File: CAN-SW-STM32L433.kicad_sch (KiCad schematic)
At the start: 8 parts, among them U1 STM32L433CCTx

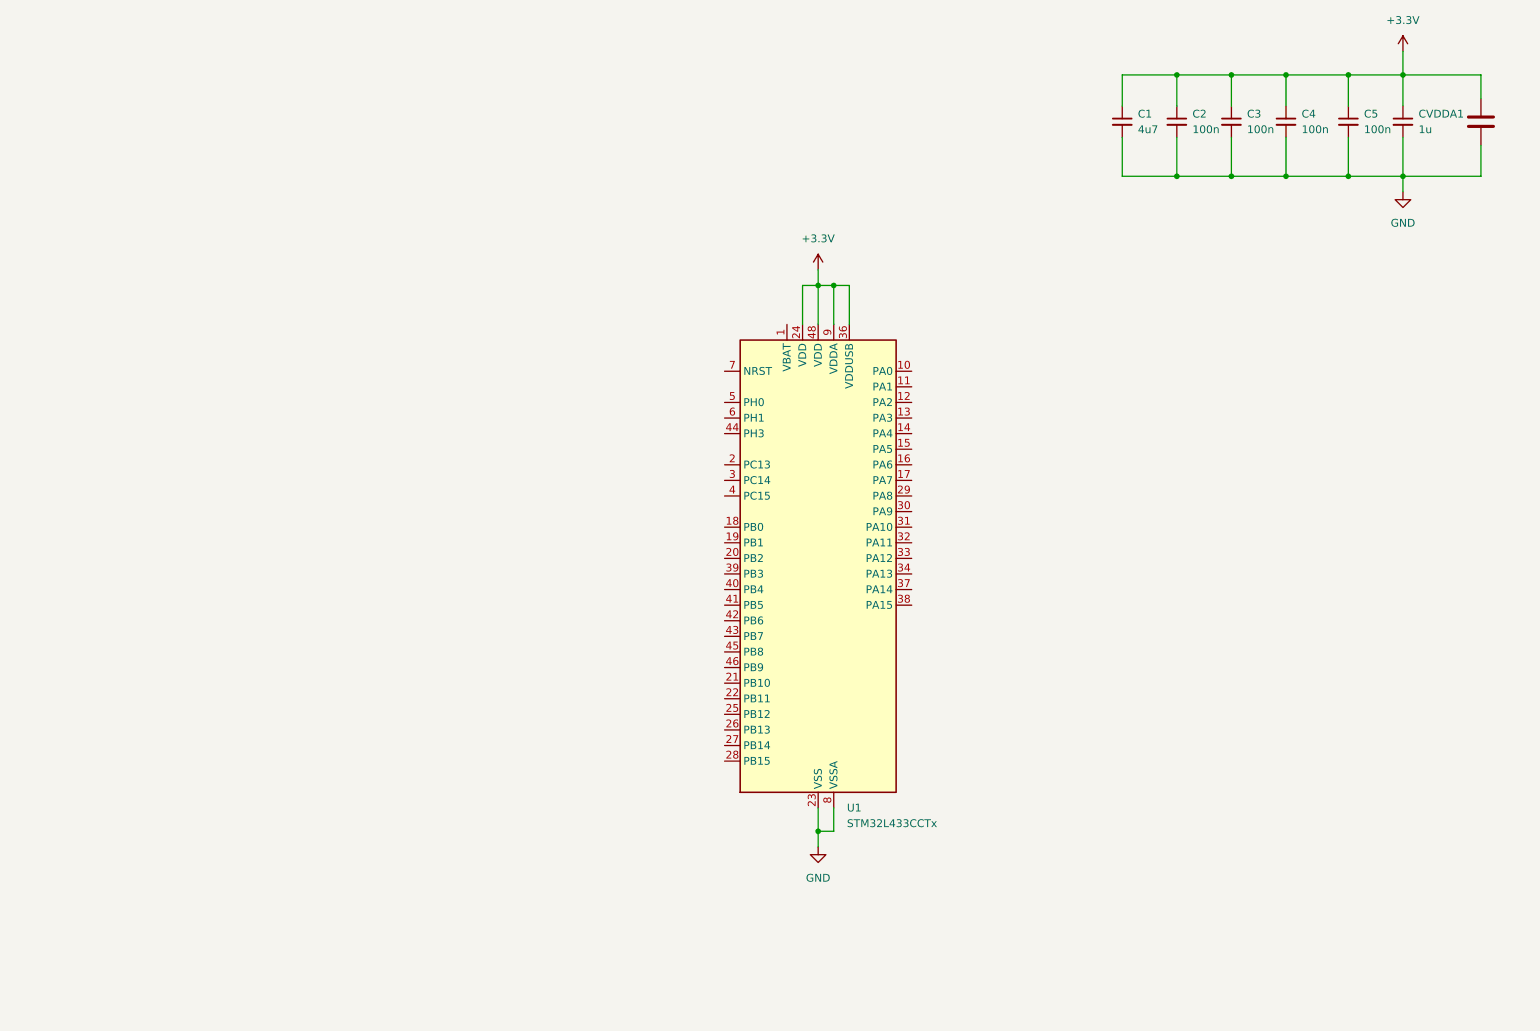
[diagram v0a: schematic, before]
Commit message: still adding parts, working on basic layout
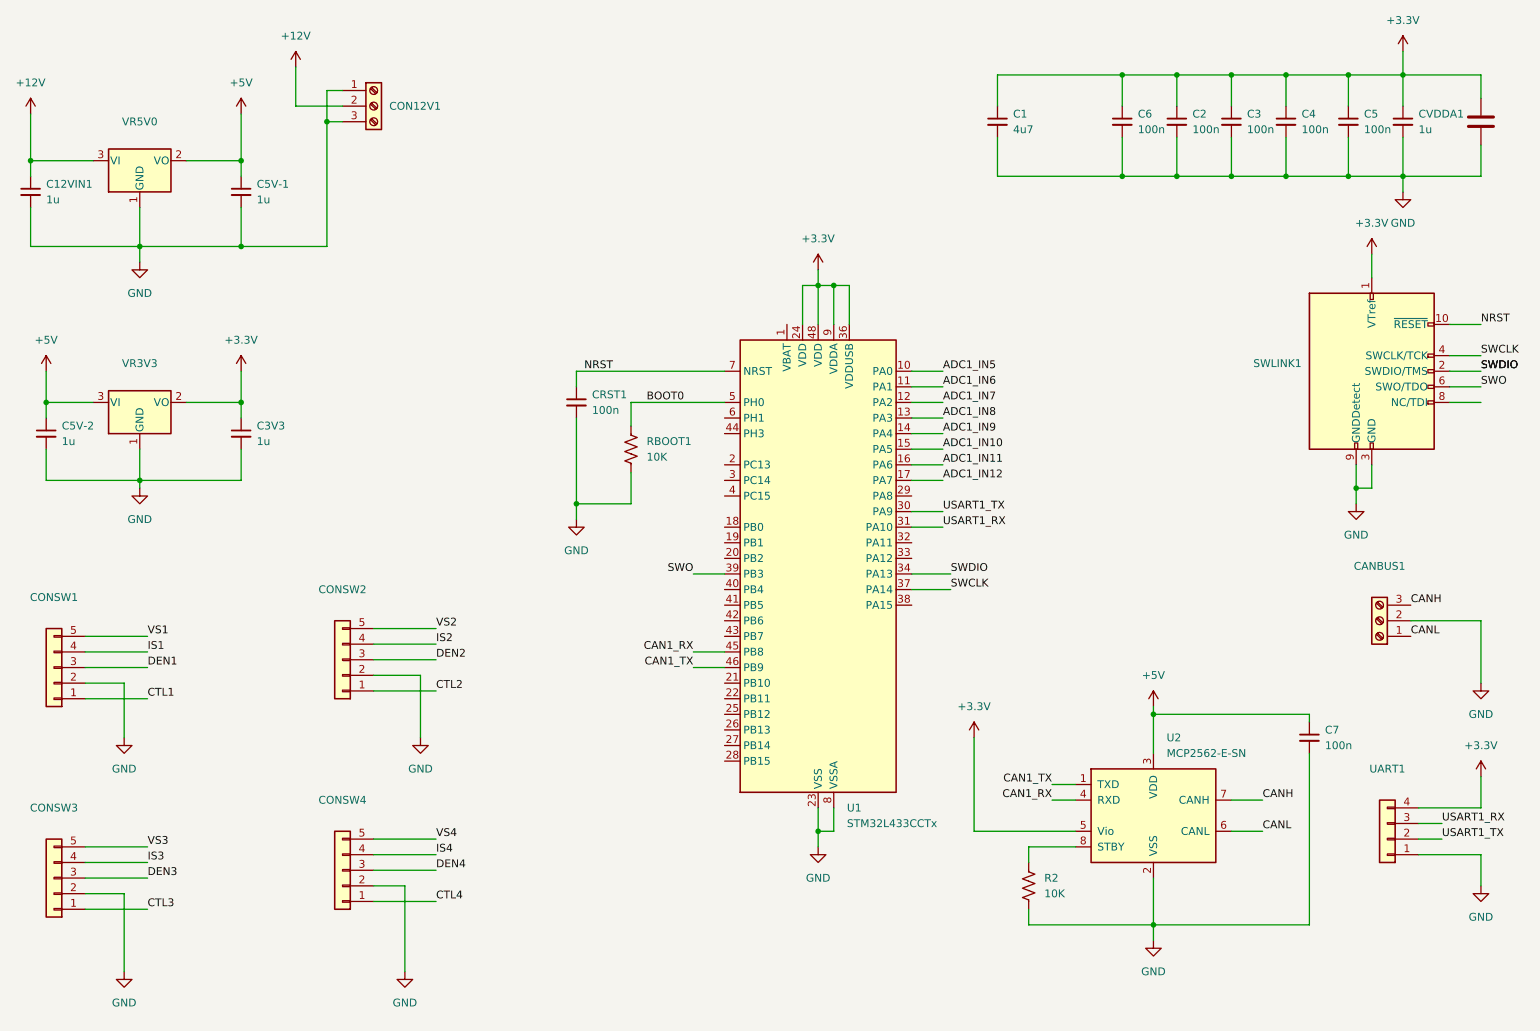
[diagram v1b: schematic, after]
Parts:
- added C12VIN1: 1u, Capacitor_SMD:C_1206_3216Metric_Pad1.33x1.80mm_HandSolder, symbol Device:C_Small
- added C3V3, C5V-1, C5V-2: 1u, Capacitor_SMD:C_0805_2012Metric_Pad1.18x1.45mm_HandSolder, symbol Device:C_Small
- added C6, C7, CRST1: 100n, Capacitor_SMD:C_0603_1608Metric_Pad1.08x0.95mm_HandSolder, symbol Device:C_Small
- added CANBUS1: Screw_Terminal_01x03, TerminalBlock_Phoenix:TerminalBlock_Phoenix_MKDS-1,5-3-5.08_1x03_P5.08mm_Horizontal, symbol Connector:Screw_Terminal_01x03
- added CON12V1: CENTER+, TerminalBlock_Phoenix:TerminalBlock_Phoenix_MKDS-1,5-3-5.08_1x03_P5.08mm_Horizontal, symbol Connector:Screw_Terminal_01x03
- added CONSW1, CONSW2, CONSW3, CONSW4: Conn_01x05, Connector_PinSocket_2.54mm:PinSocket_1x05_P2.54mm_Horizontal, symbol Connector_Generic:Conn_01x05
- added R2, RBOOT1: 10K, Resistor_SMD:R_0603_1608Metric_Pad0.98x0.95mm_HandSolder, symbol Device:R_US
- added SWLINK1: Conn_ARM_JTAG_SWD_10, Connector_PinHeader_1.27mm:PinHeader_2x05_P1.27mm_Horizontal, symbol Connector:Conn_ARM_JTAG_SWD_10
- added U2: MCP2562-E-SN, Package_SO:SOIC-8_3.9x4.9mm_P1.27mm, symbol Interface_CAN_LIN:MCP2562-E-SN
- added UART1: Conn_01x04, Connector_PinHeader_1.27mm:PinHeader_1x04_P1.27mm_Horizontal, symbol Connector_Generic:Conn_01x04
- added VR3V3: TLV1117-33, Package_TO_SOT_SMD:SOT-223-3_TabPin2, symbol Regulator_Linear:TLV1117-33
- added VR5V0: TLV1117-50, Package_TO_SOT_SMD:SOT-223-3_TabPin2, symbol Regulator_Linear:TLV1117-50
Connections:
- net +3.3V: now also C3V3.1, C6.1, SWLINK1.1 (VTref), U2.5 (Vio), UART1.4 (Pin_4), VR3V3.2 (VO)
- net GND: now also C12VIN1.2, C3V3.2, C5V-1.2, C5V-2.2, C6.2, C7.2, CANBUS1.2 (Pin_2), CON12V1.1 (Pin_1), CON12V1.3 (Pin_3), CONSW1.2 (Pin_2), CONSW2.2 (Pin_2), CONSW3.2 (Pin_2), CONSW4.2 (Pin_2), CRST1.2, R2.2, RBOOT1.2, SWLINK1.3 (GND), SWLINK1.5 (GND), SWLINK1.9 (GNDDetect), U2.2 (VSS), UART1.1 (Pin_1), VR3V3.1 (GND), VR5V0.1 (GND)
- net ADC1_IN5: now reaches U1.10 (PA0)
- net ADC1_IN6: now reaches U1.11 (PA1)
- net ADC1_IN7: now reaches U1.12 (PA2)
- net ADC1_IN8: now reaches U1.13 (PA3)
- net ADC1_IN9: now reaches U1.14 (PA4)
- net ADC1_IN10: now reaches U1.15 (PA5)
- net ADC1_IN11: now reaches U1.16 (PA6)
- net ADC1_IN12: now reaches U1.17 (PA7)
- net USART1_TX: now reaches U1.30 (PA9)
- net USART1_TX: now also UART1.2 (Pin_2)
- net USART1_RX: now reaches U1.31 (PA10)
- net USART1_RX: now also UART1.3 (Pin_3)
- net SWDIO: now reaches U1.34 (PA13)
- net SWDIO: now also SWLINK1.2 (SWDIO/TMS)
- net SWCLK: now reaches U1.37 (PA14)
- net SWCLK: now also SWLINK1.4 (SWCLK/TCK)
- net SWO: now reaches U1.39 (PB3)
- net SWO: now also SWLINK1.6 (SWO/TDO)
- net CAN1_RX: now reaches U1.45 (PB8)
- net CAN1_RX: now also U2.4 (RXD)
- net CAN1_TX: now reaches U1.46 (PB9)
- net CAN1_TX: now also U2.1 (TXD)
- net BOOT0: now reaches U1.5 (PH0)
- net BOOT0: now also RBOOT1.1
- net NRST: now reaches U1.7 (NRST)
- net NRST: now also CRST1.1, SWLINK1.10 (~{RESET})
- new net: R2.1, U2.8 (STBY)
- new net +12V: C12VIN1.1, CON12V1.2 (Pin_2), VR5V0.3 (VI)
- new net +5V: C5V-1.1, C5V-2.1, C7.1, U2.3 (VDD), VR3V3.3 (VI), VR5V0.2 (VO)
- new net CANH: CANBUS1.3 (Pin_3), U2.7 (CANH)
- new net CANL: CANBUS1.1 (Pin_1), U2.6 (CANL)
- new net CTL1: CONSW1.1 (Pin_1)
- new net CTL2: CONSW2.1 (Pin_1)
- new net CTL3: CONSW3.1 (Pin_1)
- new net CTL4: CONSW4.1 (Pin_1)
- new net DEN1: CONSW1.3 (Pin_3)
- new net DEN2: CONSW2.3 (Pin_3)
- new net DEN3: CONSW3.3 (Pin_3)
- new net DEN4: CONSW4.3 (Pin_3)
- new net IS1: CONSW1.4 (Pin_4)
- new net IS2: CONSW2.4 (Pin_4)
- new net IS3: CONSW3.4 (Pin_4)
- new net IS4: CONSW4.4 (Pin_4)
- new net VS1: CONSW1.5 (Pin_5)
- new net VS2: CONSW2.5 (Pin_5)
- new net VS3: CONSW3.5 (Pin_5)
- new net VS4: CONSW4.5 (Pin_5)
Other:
- company: (none) -> Gordon McLellan
- title: (none) -> CAN-STM32L433
- moved on the sheet: C1

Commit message: almost done adding parts, working more on layout
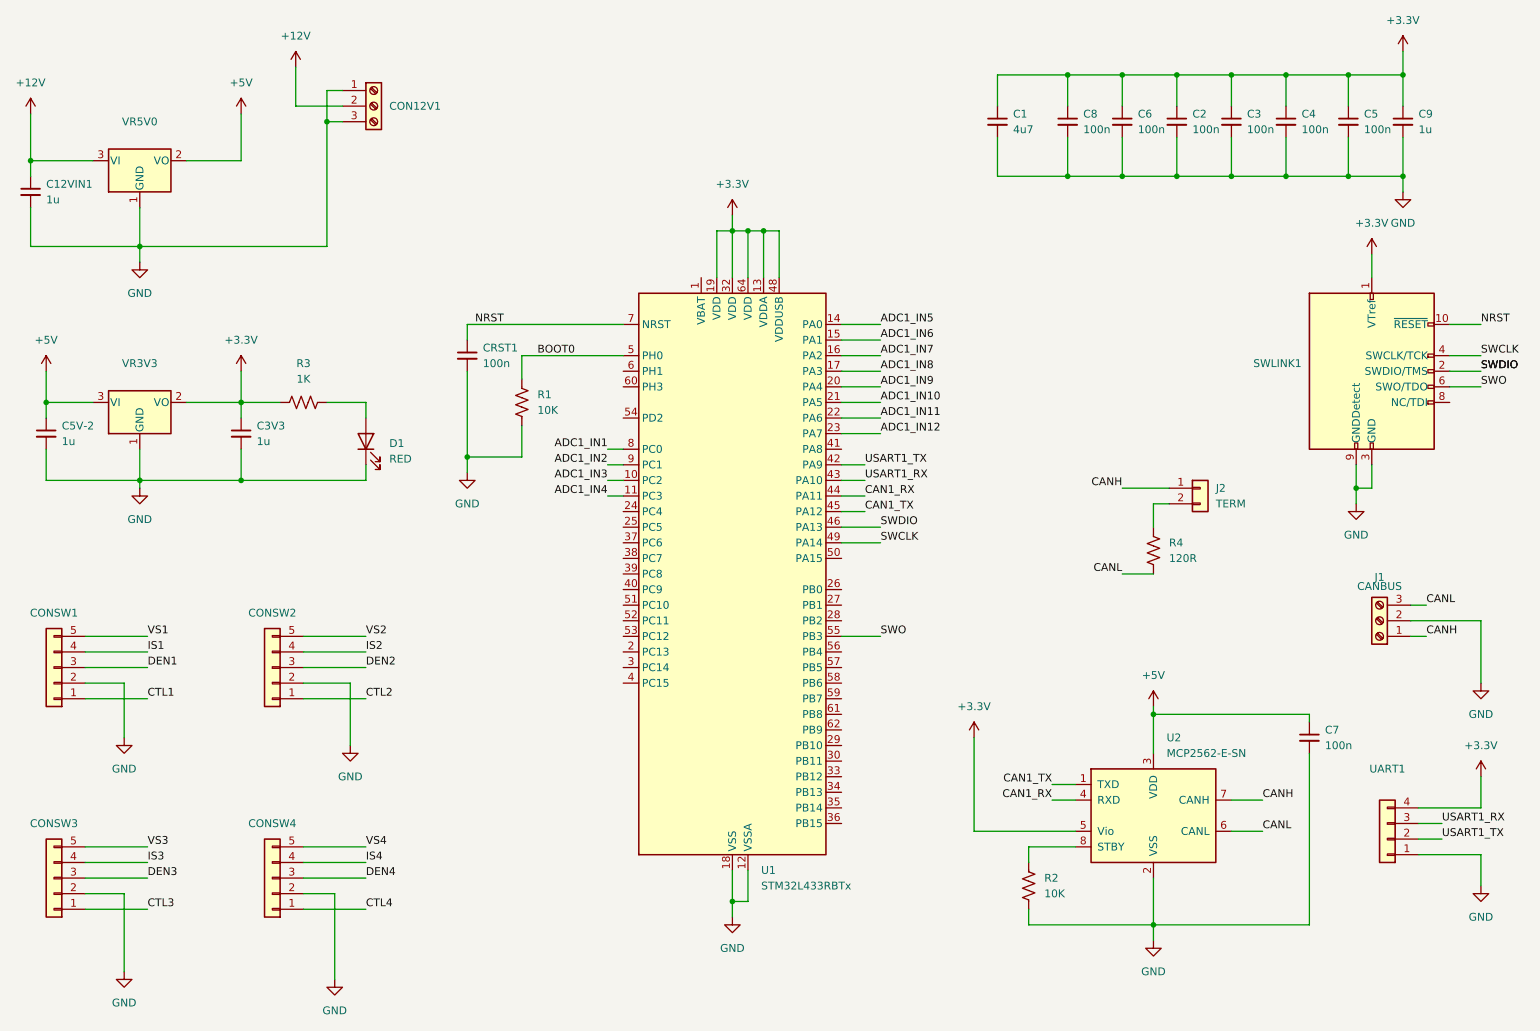
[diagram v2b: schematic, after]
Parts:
- removed C5V-1: 1u, Capacitor_SMD:C_0805_2012Metric_Pad1.18x1.45mm_HandSolder, symbol Device:C_Small
- removed CVREF1: 100n, Capacitor_SMD:C_0603_1608Metric_Pad1.08x0.95mm_HandSolder, symbol Device:C
- removed U1: STM32L433CCTx, Package_QFP:LQFP-48_7x7mm_P0.5mm, symbol MCU_ST_STM32L4:STM32L433CCTx
- added C8: 100n, Capacitor_SMD:C_0603_1608Metric_Pad1.08x0.95mm_HandSolder, symbol Device:C_Small
- added D1: RED, LED_THT:LED_D5.0mm_Clear, symbol Device:LED
- added J2: TERM, Connector_PinHeader_1.27mm:PinHeader_1x02_P1.27mm_Vertical, symbol Connector_Generic:Conn_01x02
- added R3: 1K, Resistor_SMD:R_0603_1608Metric_Pad0.98x0.95mm_HandSolder, symbol Device:R_US
- added R4: 120R, Resistor_THT:R_Axial_DIN0207_L6.3mm_D2.5mm_P7.62mm_Horizontal, symbol Device:R_US
- added U1: STM32L433RBTx, Package_QFP:LQFP-64_10x10mm_P0.5mm, symbol MCU_ST_STM32L4:STM32L433RBTx
- CON12V1: footprint TerminalBlock_Phoenix:TerminalBlock_Phoenix_MKDS-1,5-3-5.08_1x03_P5.08mm_Horizontal -> TerminalBlock_Phoenix:TerminalBlock_Phoenix_MKDS-1,5-3_1x03_P5.00mm_Horizontal
- CONSW1, CONSW2, CONSW3, CONSW4: footprint Connector_PinSocket_2.54mm:PinSocket_1x05_P2.54mm_Horizontal -> Connector_PinHeader_2.54mm:PinHeader_1x05_P2.54mm_Horizontal
- J1: renamed from CANBUS1; value Screw_Terminal_01x03 -> CANBUS; footprint TerminalBlock_Phoenix:TerminalBlock_Phoenix_MKDS-1,5-3-5.08_1x03_P5.08mm_Horizontal -> TerminalBlock_Phoenix:TerminalBlock_Phoenix_MKDS-1,5-3_1x03_P5.00mm_Horizontal
- renumbered CVDDA1 to C9, RBOOT1 to R1
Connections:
- net +3.3V: now also C8.1, R3.1, U1.13 (VDDA), U1.19 (VDD), U1.32 (VDD), U1.48 (VDDUSB), U1.64 (VDD)
- net ADC1_IN10: now also U1.21 (PA5)
- net ADC1_IN11: now also U1.22 (PA6)
- net ADC1_IN12: now also U1.23 (PA7)
- net ADC1_IN5: now also U1.14 (PA0)
- net ADC1_IN6: now also U1.15 (PA1)
- net ADC1_IN7: now also U1.16 (PA2)
- net ADC1_IN8: now also U1.17 (PA3)
- net ADC1_IN9: now also U1.20 (PA4)
- net BOOT0: now also U1.5 (PH0)
- net CAN1_RX: now also U1.44 (PA11)
- net CAN1_TX: now also U1.45 (PA12)
- net CANH: now also J1.1 (Pin_1), J2.1 (Pin_1); no longer J1.3 (Pin_3)
- net CANL: now also J1.3 (Pin_3), R4.2; no longer J1.1 (Pin_1)
- net GND: now also C8.2, D1.1 (K), U1.12 (VSSA), U1.18 (VSS), U1.31 (VSS), U1.47 (VSS), U1.63 (VSS)
- net NRST: now also U1.7 (NRST)
- net SWCLK: now also U1.49 (PA14)
- net SWDIO: now also U1.46 (PA13)
- net SWO: now also U1.55 (PB3)
- net USART1_RX: now also U1.43 (PA10)
- net USART1_TX: now also U1.42 (PA9)
- new net: J2.2 (Pin_2), R4.1
- new net: D1.2 (A), R3.2
- new net ADC1_IN1: U1.8 (PC0)
- new net ADC1_IN2: U1.9 (PC1)
- new net ADC1_IN3: U1.10 (PC2)
- new net ADC1_IN4: U1.11 (PC3)
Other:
- moved on the sheet: CONSW2, CONSW4, CRST1, R1

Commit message: more progress on the layout, fixed connector sizes for uart and swlink
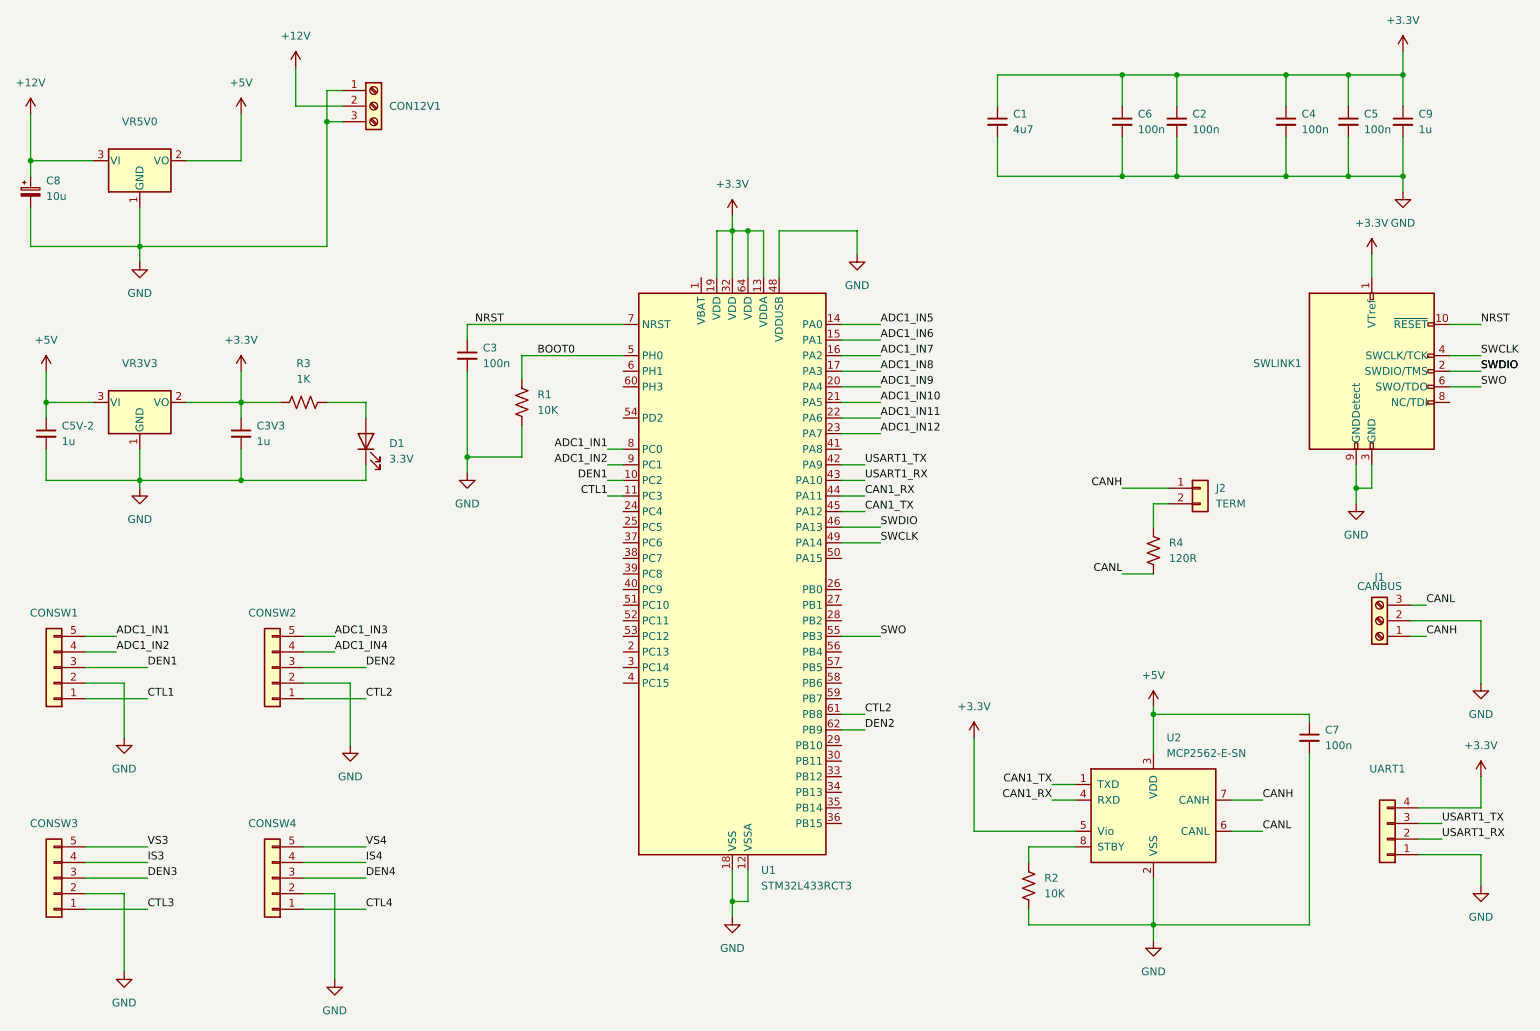
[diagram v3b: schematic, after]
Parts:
- removed C12VIN1: 1u, Capacitor_SMD:C_1206_3216Metric_Pad1.33x1.80mm_HandSolder, symbol Device:C_Small
- removed C3, C8: 100n, Capacitor_SMD:C_0603_1608Metric_Pad1.08x0.95mm_HandSolder, symbol Device:C_Small
- added C8: 10u, Capacitor_THT:CP_Radial_D5.0mm_P2.50mm, symbol Device:C_Polarized_Small
- D1: value RED -> 3.3V
- SWLINK1: footprint Connector_PinHeader_1.27mm:PinHeader_2x05_P1.27mm_Horizontal -> Connector_PinHeader_2.54mm:PinHeader_2x05_P2.54mm_Horizontal
- U1: value STM32L433RBTx -> STM32L433RCT3
- UART1: footprint Connector_PinHeader_1.27mm:PinHeader_1x04_P1.27mm_Horizontal -> Connector_PinHeader_2.54mm:PinHeader_1x04_P2.54mm_Horizontal
- renumbered CRST1 to C3
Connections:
- net IS1 is gone; now on net ADC1_IN2: CONSW1.4 (Pin_4)
- net IS2 is gone; now on net ADC1_IN4: CONSW2.4 (Pin_4)
- net VS1 is gone; now on net ADC1_IN1: CONSW1.5 (Pin_5)
- net VS2 is gone; now on net ADC1_IN3: CONSW2.5 (Pin_5)
- net +12V: now also C8.1
- net +3.3V: no longer U1.48 (VDDUSB)
- net ADC1_IN3: no longer U1.10 (PC2)
- net ADC1_IN4: no longer U1.11 (PC3)
- net CTL1: now also U1.11 (PC3)
- net CTL2: now also U1.61 (PB8)
- net DEN1: now also U1.10 (PC2)
- net DEN2: now also U1.62 (PB9)
- net GND: now also U1.48 (VDDUSB), C8.2
- net USART1_RX: now also UART1.2 (Pin_2); no longer UART1.3 (Pin_3)
- net USART1_TX: now also UART1.3 (Pin_3); no longer UART1.2 (Pin_2)

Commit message: routing getting tricky with just two layers
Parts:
- added C10, C11, C12, C13: 100n, Capacitor_SMD:C_0603_1608Metric_Pad1.08x0.95mm_HandSolder, symbol Device:C_Small
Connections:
- net ADC1_IN3 is gone; now on net ADC1_IN5: CONSW2.5 (Pin_5)
- net ADC1_IN4 is gone; now on net ADC1_IN6: CONSW2.4 (Pin_4)
- net ADC1_IN1: now also C10.1
- net ADC1_IN2: now also C11.1
- net ADC1_IN5: now also C12.1
- net ADC1_IN6: now also C13.1
- net GND: now also C10.2, C11.2, C12.2, C13.2
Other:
- moved on the sheet: J2, R4

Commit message: layout mostly complete, working on DRC
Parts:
- added C14, C15, C16, C17: 100n, Capacitor_SMD:C_0603_1608Metric_Pad1.08x0.95mm_HandSolder, symbol Device:C_Small
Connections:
- net IS3 is gone; now on net ADC1_IN9: CONSW3.4 (Pin_4)
- net IS4 is gone; now on net ADC1_IN11: CONSW4.4 (Pin_4)
- net VS3 is gone; now on net ADC1_IN10: CONSW3.5 (Pin_5)
- net VS4 is gone; now on net ADC1_IN12: CONSW4.5 (Pin_5)
- net ADC1_IN10: now also C16.1
- net ADC1_IN11: now also C15.1
- net ADC1_IN12: now also C14.1
- net ADC1_IN5: now also CONSW2.4 (Pin_4); no longer CONSW2.5 (Pin_5)
- net ADC1_IN6: now also CONSW2.5 (Pin_5); no longer CONSW2.4 (Pin_4)
- net ADC1_IN9: now also C17.1
- net CTL3: now also U1.57 (PB5)
- net CTL4: now also U1.52 (PC11)
- net DEN3: now also U1.54 (PD2)
- net DEN4: now also U1.50 (PA15)
- net GND: now also C14.2, C15.2, C16.2, C17.2
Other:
- moved on the sheet: C12, C13
